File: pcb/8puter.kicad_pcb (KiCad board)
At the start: 2 copper layers, 180 x 120 mm, 80 parts, among them J1 PWR-DC, J2 DB9_Female, J3 USB_A, SW1 RESET_SW, U1 74AHC00, U10 74AC10, U11 74AC14, U12 W65C22NxPL, U13 MX25V8035F, U14 FT240XQ, U2 74AHC74, U3 DS1135Z, U4 74AHC32, U5 74AHC125, U6 MAX811MEUS-T, U7 STM8S003K3T, U8 74AHC00, U9 74AHC02

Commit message: Pivot to 6502
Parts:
- removed U1: 74AHC00, Package_SO:TSSOP-14_4.4x5mm_P0.65mm
- removed U10: 74AC10, Package_SO:TSSOP-14_4.4x5mm_P0.65mm
- removed U4: 74AHC32, Package_SO:TSSOP-14_4.4x5mm_P0.65mm
- removed U5: 74AHC125, Package_SO:TSSOP-14_4.4x5mm_P0.65mm
- removed U9: 74AHC02, Package_SO:TSSOP-14_4.4x5mm_P0.65mm
- added C24: 100nF, Capacitor_SMD:C_0603_1608Metric, F.Cu at (190.2, 91.3)
- added C25: 100nF, Capacitor_SMD:C_0603_1608Metric, F.Cu at (190.2, 89.5)
- added C26: 100nF, Capacitor_SMD:C_0603_1608Metric, F.Cu at (190.2, 87.7)
- added C27: 10nF, Capacitor_SMD:C_0603_1608Metric, F.Cu at (190.2, 85.9)
- added C28: 100nF, Capacitor_SMD:C_0603_1608Metric, F.Cu at (190.1, 84.2)
- added C29: 10nF, Capacitor_SMD:C_0603_1608Metric, F.Cu at (190.1, 82.4)
- added C30: 10nF, Capacitor_SMD:C_0603_1608Metric, F.Cu at (190.1, 80.7)
- added C31: 10nF, Capacitor_SMD:C_0603_1608Metric, F.Cu at (190.1, 78.8)
- added J4: FPGA_Prog, Connector_PinHeader_1.00mm:PinHeader_1x05_P1.00mm_Vertical, F.Cu at (181.8, 92.7)
- added PWREG1: LT1962-3.3, Package_SO:MSOP-8_3x3mm_P0.65mm, F.Cu at (108.8, 61.7)
- added R8: 4.7K, Resistor_SMD:R_0603_1608Metric, F.Cu at (184.0, 90.6)
- added R9: 1K, Resistor_SMD:R_0402_1005Metric, F.Cu at (182.4, 95.2)
- added U15: LCMXO2-256ZE-3SG32I, Package_DFN_QFN:QFN-32-1EP_5x5mm_P0.5mm_EP3.1x3.1mm, F.Cu at (176.5, 93.0)
- C1: value 1uF -> 10uF
- C19, C20: value 10nF -> 100nF; footprint Capacitor_SMD:C_0603_1608Metric -> Capacitor_THT:CP_Radial_D5.0mm_P2.00mm
- C21: value 10nF -> 100nF
- C5, C6: value 10nF -> 10uF; footprint Capacitor_SMD:C_0603_1608Metric -> Capacitor_THT:CP_Radial_D5.0mm_P2.00mm
- C7, C8: value 10nF -> 1uF; footprint Capacitor_SMD:C_0603_1608Metric -> Capacitor_THT:CP_Radial_D5.0mm_P2.00mm
- ROM1: value AT28HC256 -> AT28C256
- SRAM1: value KM62256CLP -> AS6C62256-55PCN
- U3: value DS1135Z -> DS1135Z-6+
- moved C8 109.7 mm to (88.2, 83.8), turned to -90 degrees
- moved C20 109.0 mm to (93.8, 60.7)
- moved C5 100.9 mm to (98.1, 83.5), turned to -90 degrees
- moved C19 100.7 mm to (103.3, 60.7)
- moved C7 94.2 mm to (115.8, 53.7), turned to -90 degrees
- moved C6 91.3 mm to (115.8, 61.2), turned to -90 degrees
- moved CRYSTAL0 79.9 mm to (192.1, 63.9), turned to 180 degrees
- moved C21 75.2 mm to (127.6, 65.3), turned to 0 degrees
- moved C11 74.3 mm to (130.8, 74.8)
- moved C18 71.3 mm to (132.0, 46.0)
- moved C2 68.4 mm to (132.1, 52.0), turned to 0 degrees
- moved C12 67.5 mm to (132.0, 57.2), turned to 0 degrees
- moved C14 66.0 mm to (113.0, 74.7)
- moved R4 60.0 mm to (142.0, 56.2), turned to 180 degrees
- moved R2 55.1 mm to (142.1, 53.3), turned to 180 degrees
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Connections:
- net Net-(D1-Pad1) renamed /Bus Control/RDY_R
- BDT1 pad 1: Net-(BDT1-Pad1) -> /Bus Control/CPU_W~{R}
- C17 pad 1: +5V -> Net-(C17-Pad1)
- C19 pad 1: +5V -> Net-(C19-Pad1)
- C20 pad 1: +5V -> Net-(C17-Pad1)
- C5 pad 1: +5V -> /Power/PWR
- C6 pad 1: +5V -> Net-(C19-Pad1)
- C7 pad 1: +5V -> Net-(C19-Pad1)
- C8 pad 1: +5V -> Net-(C17-Pad1)
- PWREG2 pad 1: +5V -> Net-(C17-Pad1)
- RP2 pad 2: ADDR11 -> ADDR8
- RP2 pad 3: ADDR10 -> ADDR9
- RP2 pad 4: ADDR9 -> ADDR11
- RP2 pad 5: ADDR8 -> ADDR10
- U12 pad 27: CLOCK -> /Peripheral Handler/CLK
- U2 pad 14: +5V -> (no net)
- U2 pad 7: GND -> (no net)
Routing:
- net ADDR19: track 136.2 -> 15.0 mm
- net ADDR18: track 131.1 -> 16.4 mm
- net CLOCK: track 127.1 -> 17.4 mm, vias 4 -> 0
- net ADDR17: track 125.7 -> 17.6 mm
- net ADDR16: track 120.9 -> 18.9 mm
- net /Bus Control/CLK=: track 107.0 -> 12.8 mm, vias 3 -> 0
- net ADDR15: track 104.0 -> 13.6 mm, vias 3 -> 0
- net +5V: track 77.5 -> 4.05 mm, vias 6 -> 0
- net BE: track 70.6 -> 7.28 mm, vias 2 -> 0
- net ADDR23: track 53.6 -> 10.2 mm, vias 2 -> 0
- net RDY: track 43.0 -> 0.00 mm, vias 2 -> 0
- net /Memory Unit/~{ERAM_CS0}: track 42.3 -> 0.00 mm
- net /Bus Control/CLK+: track 55.7 -> 14.6 mm, vias 2 -> 0
- net DATA0: track 85.6 -> 126.7 mm, vias 1 -> 4
- net ADDR22: track 50.4 -> 11.3 mm, vias 2 -> 0
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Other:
- outline, holes or cut-outs redrawn

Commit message: Serial interface
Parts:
- removed AD_DEC1: 74HCT154, Package_SO:SO-24_5.3x15mm_P1.27mm
- removed BDT1: 74AC245, Package_SO:TSSOP-20_4.4x6.5mm_P0.65mm
- removed C13, C14: 1uF, Capacitor_THT:CP_Radial_D8.0mm_P3.80mm
- removed C18: 100nF, Capacitor_SMD:C_1206_3216Metric_Pad1.33x1.80mm_HandSolder
- removed C21, C24, C25, C26, C28: 100nF, Capacitor_SMD:C_0603_1608Metric
- removed C22, C27, C29, C30, C31: 10nF, Capacitor_SMD:C_0603_1608Metric
- removed the C3 at (77.1, 74.2)
- removed the C3 at (87.1, 74.2)
- removed D1: 1N5817, Diode_THT:D_A-405_P7.62mm_Horizontal
- removed ERAM0, ERAM1, ERAM2, ERAM3: IS62WV10248, Package_SO:TSOP-II-44_10.16x18.41mm_P0.8mm
- removed J4: FPGA_Prog, Connector_PinHeader_1.00mm:PinHeader_1x05_P1.00mm_Vertical
- removed LATCH1: 74AC573, Package_SO:TSSOP-20_4.4x6.5mm_P0.65mm
- removed R12, R13, R14, R15, R16, R17, R18, R19, R20, R21, R22, R23, R32, R33, R34, R35, R6, R7: 1K, Resistor_SMD:R_0603_1608Metric
- removed R4, R5: 10K, Resistor_SMD:R_1206_3216Metric_Pad1.30x1.75mm_HandSolder
- removed R8: 4.7K, Resistor_SMD:R_0603_1608Metric
- removed R9: 1K, Resistor_SMD:R_0402_1005Metric
- removed RP1, RP2: 1K, Resistor_THT:R_Array_SIP9
- removed SRAM1: AS6C62256-55PCN, Package_DIP:DIP-28_W15.24mm
- removed SW1: RESET_SW, Button_Switch_THT:SW_PUSH_6mm_H13mm
- removed U11: 74AC14, Package_SO:TSSOP-14_4.4x5mm_P0.65mm
- removed U12: W65C22NxPL, Package_QFP:PQFP-44_10x10mm_P0.8mm
- removed U13: MX25V8035F, Package_SO:SOP-8_3.9x4.9mm_P1.27mm
- removed U14: FT240XQ, Package_DFN_QFN:QFN-24-1EP_4x4mm_P0.5mm_EP2.6x2.6mm
- removed U15: LCMXO2-256ZE-3SG32I, Package_DFN_QFN:QFN-32-1EP_5x5mm_P0.5mm_EP3.1x3.1mm
- removed U3: DS1135Z-6+, Package_SO:SO-8_5.3x6.2mm_P1.27mm
- removed U7: STM8S003K3T, Package_QFP:LQFP-32_7x7mm_P0.8mm
- removed U8: 74AHC00, Package_SO:TSSOP-14_4.4x5mm_P0.65mm
- added C3: 10uF 16V, Capacitor_THT:CP_Radial_D8.0mm_P5.00mm, F.Cu at (112.7, 47.8)
- added GLUE_FPGA1: LCMXO2-256-QFN32, Package_DFN_QFN:QFN-32-1EP_5x5mm_P0.5mm_EP3.1x3.1mm, F.Cu at (178.1, 114.8)
- added JTAG1: PIN_HDR, Connector_PinHeader_1.00mm:PinHeader_1x05_P1.00mm_Vertical, F.Cu at (183.8, 114.5)
- added PRP1: W65C22SxQ, Package_QFP:PQFP-44_10x10mm_P0.8mm, F.Cu at (184.6, 78.0)
- added RAM1: AS6C62256-55PCN, Package_DIP:DIP-28_W15.24mm_LongPads, F.Cu at (111.6, 121.1)
- added RESET_SW1: PUSHBTN, Button_Switch_THT:SW_PUSH_6mm_H13mm, F.Cu at (148.6, 58.8)
- added SERC1: W65C51NxQ, Package_QFP:LQFP-32_7x7mm_P0.8mm, F.Cu at (114.4, 68.9)
- added SERIAL1: Conn_2Rows-11Pins, Connector_PinHeader_1.00mm:PinHeader_2x06_P1.00mm_Vertical, F.Cu at (95.7, 64.0)
- added USB1: FT240XQ, Package_DFN_QFN:QFN-24-1EP_4x4mm_P0.5mm_EP2.6x2.6mm, F.Cu at (191.6, 55.9)
- added VIDEO1: STM32F301C6Tx, Package_QFP:LQFP-48_7x7mm_P0.5mm, F.Cu at (164.4, 54.0)
- C10, C11, C15, C16, C4, C9: footprint Capacitor_SMD:C_1206_3216Metric_Pad1.33x1.80mm_HandSolder -> Capacitor_SMD:C_0805_2012Metric
- C12: value 1uF -> 100nF; footprint Capacitor_SMD:C_1210_3225Metric_Pad1.33x2.70mm_HandSolder -> Capacitor_SMD:C_0805_2012Metric
- C17, C19, C20, C6, C7, C8: footprint Capacitor_THT:CP_Radial_D5.0mm_P2.00mm -> Capacitor_SMD:C_0805_2012Metric
- C2: footprint Capacitor_SMD:C_1210_3225Metric_Pad1.33x2.70mm_HandSolder -> Capacitor_SMD:C_0805_2012Metric
- C23: footprint Capacitor_SMD:C_1206_3216Metric -> Capacitor_SMD:C_0805_2012Metric
- CPU1: value W65C816SxP -> W65C02SxP
- J2: value DB9_Female -> DB15_Female; footprint Connector_Dsub:DSUB-9_Female_Horizontal_P2.77x2.84mm_EdgePinOffset9.90mm_Housed_MountingHolesOffset11.32mm -> Connector_Dsub:DSUB-15-HD_Female_Horizontal_P2.29x1.98mm_EdgePinOffset3.03mm_Housed_MountingHolesOffset4.94mm
- R1: footprint Resistor_SMD:R_0603_1608Metric -> Resistor_SMD:R_0805_2012Metric
- R2: footprint Resistor_SMD:R_1206_3216Metric_Pad1.30x1.75mm_HandSolder -> Resistor_SMD:R_0805_2012Metric
- R3: value 10K -> 4.7K; footprint Resistor_SMD:R_1206_3216Metric_Pad1.30x1.75mm_HandSolder -> Resistor_SMD:R_0805_2012Metric
- ROM1: footprint Package_DIP:DIP-28_W15.24mm_LongPads -> Package_DIP:DIP-28_W15.24mm_Socket_LongPads
- moved C5 100.2 mm to (190.2, 123.0)
- moved C19 99.2 mm to (191.2, 106.6), turned to 0 degrees
- moved PWREG1 98.1 mm to (189.3, 117.7), turned to -90 degrees
- moved C7 93.9 mm to (191.2, 109.6), turned to 0 degrees
- moved C6 91.3 mm to (191.2, 112.6), turned to 0 degrees
- moved C10 77.6 mm to (107.3, 67.7), turned to -90 degrees
- moved R2 77.2 mm to (119.4, 127.1), turned to 0 degrees
- moved C9 76.8 mm to (141.0, 51.7), turned to 0 degrees
- moved CRYSTAL0 74.7 mm to (121.4, 39.8), turned to -90 degrees
- moved R3 67.7 mm to (186.1, 112.3), turned to 90 degrees
- moved C23 63.0 mm to (196.2, 55.6), turned to -90 degrees
- moved R1 55.9 mm to (182.3, 118.9)
- moved U2 53.5 mm to (137.2, 55.7), turned to 0 degrees
- moved J2 46.0 mm to (158.4, 43.2)
- moved C2 39.9 mm to (143.2, 90.3), turned to 90 degrees
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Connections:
- net RESET renamed ~{RESET}
- C10 pad 1: +5V -> GND
- C10 pad 2: GND -> +5V
- C12 pad 1: +5V -> GND
- C12 pad 2: GND -> +5V
- C19 pad 1: Net-(C19-Pad1) -> +3V3
- C5 pad 1: /Power/PWR -> +5V
- C6 pad 1: Net-(C19-Pad1) -> +3V3
- C7 pad 1: Net-(C19-Pad1) -> +3V3
- CPU1 pad 26: /DBA7 -> DATA7
- CPU1 pad 27: /DBA6 -> DATA6
- CPU1 pad 28: /DBA5 -> DATA5
- CPU1 pad 29: /DBA4 -> DATA4
- CPU1 pad 3: Net-(CPU1-Pad3) -> unconnected-(CPU1-Pad3)
- CPU1 pad 30: /DBA3 -> DATA3
- CPU1 pad 31: /DBA2 -> DATA2
- CPU1 pad 32: /DBA1 -> DATA1
- CPU1 pad 33: /DBA0 -> DATA0
- CPU1 pad 35: EMU -> unconnected-(CPU1-Pad35)
- CPU1 pad 38: unconnected-(CPU1-Pad38) -> +5V
- CPU1 pad 39: VDA -> unconnected-(CPU1-Pad39)
- CPU1 pad 7: VPA -> unconnected-(CPU1-Pad7)
- J3 pad 2: unconnected-(J3-Pad2) -> Net-(J3-Pad2)
- J3 pad 3: unconnected-(J3-Pad3) -> Net-(J3-Pad3)
- J3 pad 4: unconnected-(J3-Pad4) -> GND
- J3 pad 5: unconnected-(J3-Pad5) -> GND
- PWREG1 pad 1: Net-(C19-Pad1) -> +3V3
- PWREG1 pad 4: unconnected-(PWREG1-Pad4) -> GND
- PWREG1 pad 8: /Power/PWR -> +5V
- R1 pad 1: +5V -> Net-(R1-Pad1)
- R1 pad 2: RDY -> +3V3
- R3 pad 1: +5V -> /TCK
- R3 pad 2: Net-(R3-Pad2) -> GND
- ROM1 pad 20: /Memory Unit/~{ROM_CS} -> ~{RAM_CS}
- ROM1 pad 22: ~{READ} -> CPU_W~{R}
- U2 pad 11: /Clock/CRYSTAL -> GND
- U2 pad 12: ~{CLOCK} -> GND
- U2 pad 14: (no net) -> +5V
- U2 pad 2: Net-(R3-Pad2) -> ~{CLOCK}
- U2 pad 3: /Bus Control/CLK= -> /Clock/CRYSTAL
- U2 pad 5: /Bus Control/RDY_R -> CLOCK
- U2 pad 6: /Bus Control/~{RDY_R} -> ~{CLOCK}
- U2 pad 7: (no net) -> GND
- U2 pad 8: ~{CLOCK} -> unconnected-(U2-Pad8)
- U2 pad 9: CLOCK -> unconnected-(U2-Pad9)
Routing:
- net CPU_R~{W}: track 6.61 -> 185.1 mm, vias 0 -> 2
- net ADDR1: track 0.00 -> 176.1 mm, vias 0 -> 3
- net ADDR0: track 0.00 -> 173.2 mm, vias 0 -> 3
- net ~{SERIAL_CS}: track 0.00 -> 166.8 mm, vias 0 -> 4
- net CPU_W~{R}: track 0.00 -> 147.3 mm, vias 0 -> 3
- net ~{ROM_CS}: track 0.00 -> 143.5 mm, vias 0 -> 2
- net ADDR10: track 0.00 -> 139.0 mm, vias 0 -> 4
- net ADDR11: track 0.00 -> 130.4 mm, vias 0 -> 4
- net ADDR9: track 0.00 -> 125.3 mm, vias 0 -> 4
- net ~{RAM_CS}: track 0.00 -> 121.9 mm, vias 0 -> 2
- net ADDR15: track 13.6 -> 130.2 mm, vias 0 -> 3
- net ADDR13: track 7.78 -> 120.5 mm, vias 0 -> 3
- net ADDR8: track 0.00 -> 112.2 mm, vias 0 -> 4
- net ADDR2: track 0.00 -> 100.3 mm, vias 0 -> 1
- net ADDR3: track 0.00 -> 94.9 mm, vias 0 -> 1
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- added copper zone on B.Cu, net +5V
- added copper zone on F.Cu, net GND
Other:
- board size 180 x 120 mm -> 120 x 100 mm

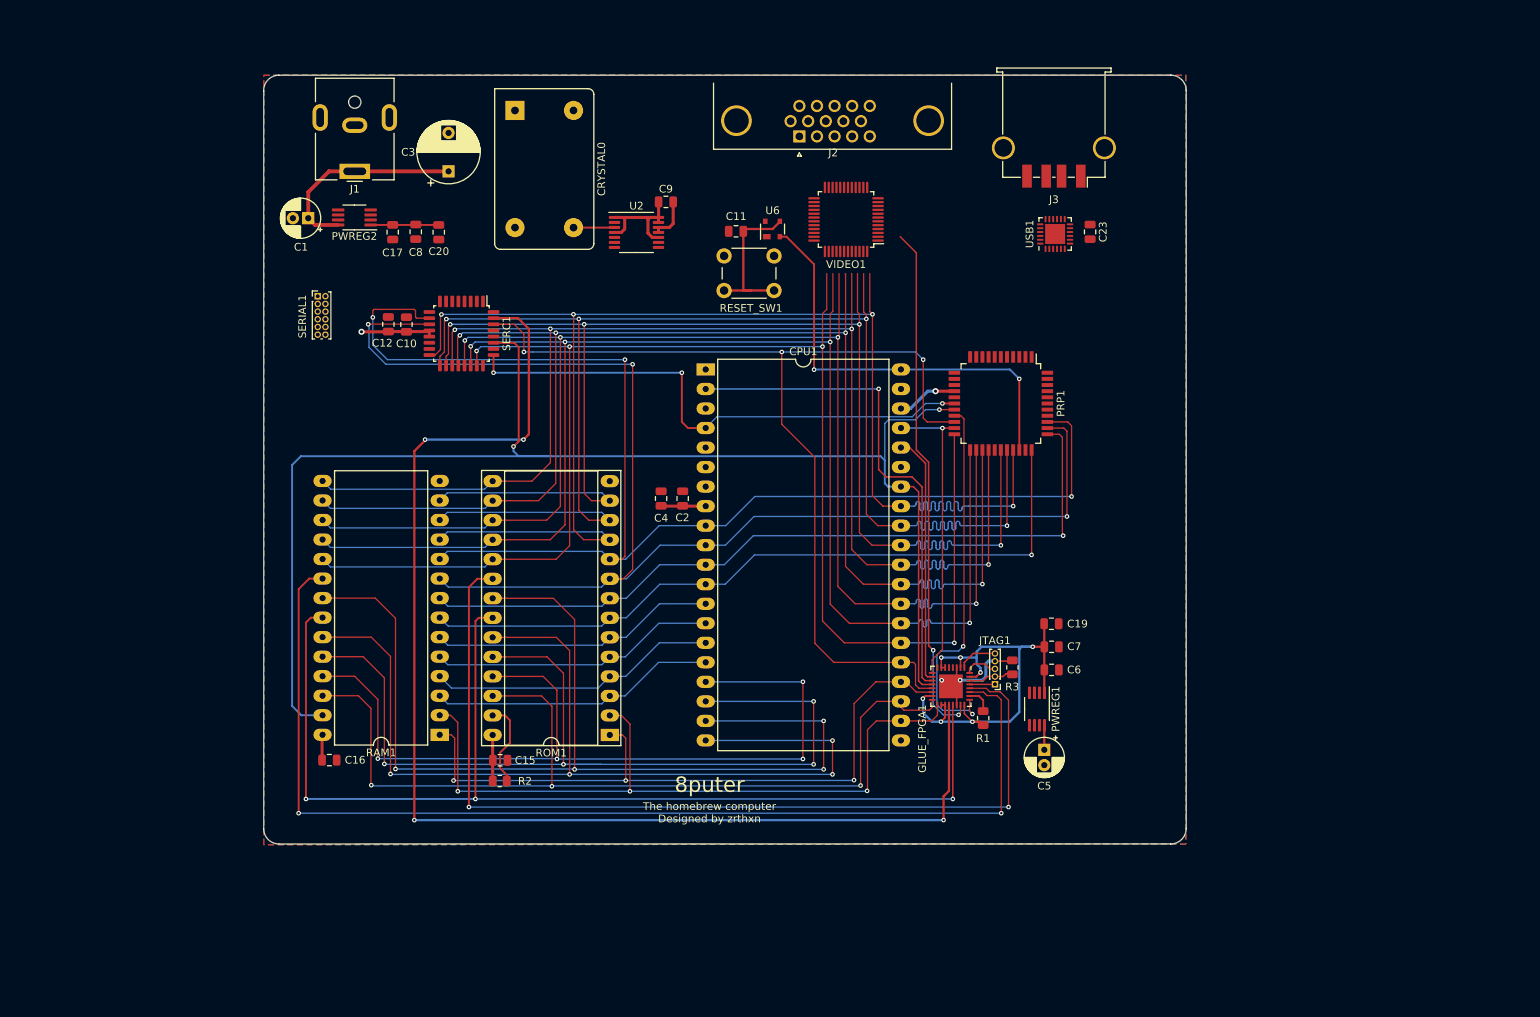
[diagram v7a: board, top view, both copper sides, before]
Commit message: Serial, debug and prph headers
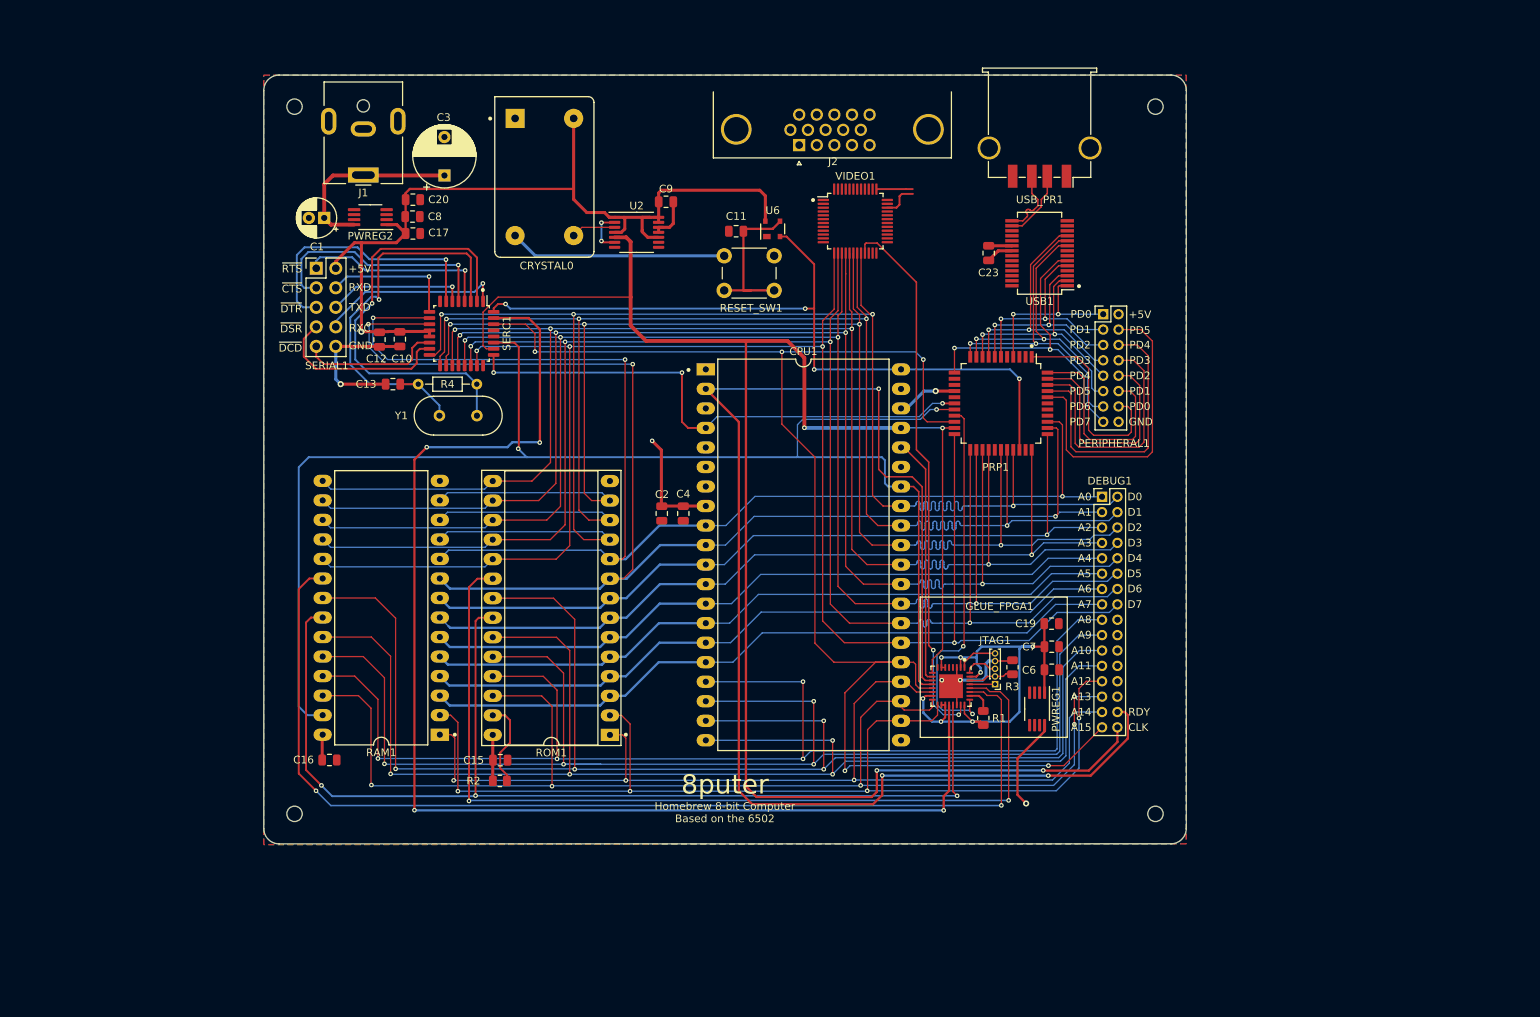
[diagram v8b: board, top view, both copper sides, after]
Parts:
- removed C5: 10uF, Capacitor_THT:CP_Radial_D5.0mm_P2.00mm
- removed J3: USB_A, Connector_USB:USB_A_TE_292303-7_Horizontal
- added C13: 30pF, Capacitor_SMD:C_0805_2012Metric, F.Cu at (105.5, 75.4)
- added DEBUG1: Conn_02x16_Odd_Even, Connector_PinHeader_2.00mm:PinHeader_2x16_P2.00mm_Vertical, F.Cu at (197.7, 90.1)
- added PERIPHERAL1: Conn_02x08_Odd_Even, Connector_PinHeader_2.00mm:PinHeader_2x08_P2.00mm_Vertical, F.Cu at (197.9, 66.3)
- added R4: 1M, Resistor_THT:R_Axial_DIN0204_L3.6mm_D1.6mm_P7.62mm_Horizontal, F.Cu at (116.4, 75.4)
- added USB_PR1: USB_A, Connector_USB:USB_A_TE_292303-7_Horizontal, F.Cu at (189.6, 42.0)
- added Y1: 1.8432MHz, Crystal:Crystal_HC49-4H_Vertical, F.Cu at (111.5, 79.5)
- SERIAL1: value Conn_2Rows-11Pins -> Conn_02x05_Odd_Even; footprint Connector_PinHeader_1.00mm:PinHeader_2x06_P1.00mm_Vertical -> Connector_PinHeader_2.54mm:PinHeader_2x05_P2.54mm_Vertical
- USB1: value FT240XQ -> FT245RL; footprint Package_DFN_QFN:QFN-24-1EP_4x4mm_P0.5mm_EP2.6x2.6mm -> Package_SO:SSOP-28_5.3x10.2mm_P0.65mm
- moved C23 13.5 mm to (183.0, 58.4)
- moved C20 5.41 mm to (108.1, 51.4), turned to 0 degrees
- moved SERIAL1 3.64 mm to (95.5, 60.4)
- moved C4 3.48 mm to (143.3, 92.3), turned to -90 degrees
- moved C2 3.34 mm to (140.5, 92.3), turned to -90 degrees
- moved USB1 3.22 mm to (189.6, 58.4), turned to 180 degrees
- moved C17 2.64 mm to (108.1, 55.8), turned to 0 degrees
- moved C12 2.30 mm to (103.7, 69.6), turned to 90 degrees
- moved C10 2.09 mm to (106.4, 69.6), turned to 90 degrees
- moved C1 2.08 mm to (96.6, 53.8)
- moved PWREG2 2.08 mm to (102.6, 53.7)
- moved C8 2.02 mm to (108.0, 53.6), turned to 0 degrees
- moved VIDEO1 1.22 mm to (165.6, 54.2), turned to 0 degrees
- moved J1 1.22 mm to (101.6, 48.2)
- moved J2 1.13 mm to (158.3, 44.3)
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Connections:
- C17 pad 1: Net-(C17-Pad1) -> +5V
- C20 pad 1: Net-(C17-Pad1) -> +5V
- C8 pad 1: Net-(C17-Pad1) -> +5V
- PRP1 pad 1: unconnected-(PRP1-Pad1) -> /Peripheral Handler/PC5
- PRP1 pad 2: unconnected-(PRP1-Pad2) -> Net-(PRP1-Pad2)
- PRP1 pad 3: unconnected-(PRP1-Pad3) -> Net-(PRP1-Pad3)
- PRP1 pad 40: unconnected-(PRP1-Pad40) -> /Peripheral Handler/PC0
- PRP1 pad 41: unconnected-(PRP1-Pad41) -> /Peripheral Handler/PC1
- PRP1 pad 42: unconnected-(PRP1-Pad42) -> /Peripheral Handler/PC2
- PRP1 pad 43: unconnected-(PRP1-Pad43) -> /Peripheral Handler/PC3
- PRP1 pad 44: unconnected-(PRP1-Pad44) -> /Peripheral Handler/PC4
- PWREG2 pad 1: Net-(C17-Pad1) -> +5V
- SERC1 pad 1: unconnected-(SERC1-Pad1) -> Net-(SERC1-Pad1)
- SERC1 pad 14: unconnected-(SERC1-Pad14) -> Net-(SERC1-Pad14)
- SERC1 pad 15: unconnected-(SERC1-Pad15) -> Net-(SERC1-Pad15)
- SERC1 pad 2: unconnected-(SERC1-Pad2) -> Net-(R4-Pad1)
- SERC1 pad 3: unconnected-(SERC1-Pad3) -> Net-(C13-Pad1)
- SERC1 pad 4: unconnected-(SERC1-Pad4) -> Net-(SERC1-Pad4)
- SERC1 pad 5: unconnected-(SERC1-Pad5) -> Net-(SERC1-Pad5)
- SERC1 pad 6: unconnected-(SERC1-Pad6) -> Net-(SERC1-Pad6)
- SERC1 pad 7: unconnected-(SERC1-Pad7) -> Net-(SERC1-Pad7)
- SERC1 pad 9: unconnected-(SERC1-Pad9) -> Net-(SERC1-Pad9)
- SERIAL1 pad 1: unconnected-(SERIAL1-Pad1) -> Net-(SERC1-Pad4)
- SERIAL1 pad 10: unconnected-(SERIAL1-Pad10) -> GND
- SERIAL1 pad 2: unconnected-(SERIAL1-Pad2) -> +5V
- SERIAL1 pad 3: unconnected-(SERIAL1-Pad3) -> Net-(SERC1-Pad5)
- SERIAL1 pad 4: unconnected-(SERIAL1-Pad4) -> Net-(SERC1-Pad9)
- SERIAL1 pad 5: unconnected-(SERIAL1-Pad5) -> Net-(SERC1-Pad7)
- SERIAL1 pad 6: unconnected-(SERIAL1-Pad6) -> Net-(SERC1-Pad6)
- SERIAL1 pad 7: unconnected-(SERIAL1-Pad7) -> Net-(SERC1-Pad15)
- SERIAL1 pad 8: unconnected-(SERIAL1-Pad8) -> Net-(SERC1-Pad1)
- SERIAL1 pad 9: unconnected-(SERIAL1-Pad9) -> Net-(SERC1-Pad14)
- USB1 pad 1: /Peripheral Handler/PD1 -> /Peripheral Handler/PD0
- USB1 pad 10: Net-(J3-Pad3) -> /Peripheral Handler/PD6
- USB1 pad 11: Net-(J3-Pad2) -> /Peripheral Handler/PD3
- USB1 pad 12: Net-(USB1-Pad12) -> unconnected-(USB1-Pad12)
- USB1 pad 13: ~{RESET} -> unconnected-(USB1-Pad13)
- USB1 pad 15: +5V -> /Peripheral Handler/SUSB+
- USB1 pad 16: GND -> /Peripheral Handler/SUSB-
- USB1 pad 18: unconnected-(USB1-Pad18) -> GND
- USB1 pad 2: /Peripheral Handler/PD7 -> /Peripheral Handler/PD4
- USB1 pad 20: unconnected-(USB1-Pad20) -> +5V
- USB1 pad 21: /Peripheral Handler/PD0 -> GND
- USB1 pad 22: /Peripheral Handler/PD4 -> unconnected-(USB1-Pad22)
- USB1 pad 23: /Peripheral Handler/PD2 -> unconnected-(USB1-Pad23)
- USB1 pad 24: Net-(USB1-Pad12) -> unconnected-(USB1-Pad24)
- USB1 pad 25: GND -> unconnected-(USB1-Pad25)
- USB1 pad 3: GND -> /Peripheral Handler/PD2
- USB1 pad 4: /Peripheral Handler/PD5 -> unconnected-(USB1-Pad4)
- USB1 pad 5: /Peripheral Handler/PD6 -> /Peripheral Handler/PD1
- USB1 pad 6: /Peripheral Handler/PD3 -> /Peripheral Handler/PD7
- USB1 pad 7: unconnected-(USB1-Pad7) -> GND
- USB1 pad 9: unconnected-(USB1-Pad9) -> /Peripheral Handler/PD5
- VIDEO1 pad 13: unconnected-(VIDEO1-Pad13) -> DATA7
- VIDEO1 pad 14: unconnected-(VIDEO1-Pad14) -> DATA6
- VIDEO1 pad 15: unconnected-(VIDEO1-Pad15) -> DATA5
- VIDEO1 pad 16: unconnected-(VIDEO1-Pad16) -> DATA4
- VIDEO1 pad 17: unconnected-(VIDEO1-Pad17) -> DATA3
- VIDEO1 pad 18: DATA0 -> DATA2
- VIDEO1 pad 2: ~{VID_CS} -> unconnected-(VIDEO1-Pad2)
- VIDEO1 pad 20: DATA2 -> DATA0
- VIDEO1 pad 21: unconnected-(VIDEO1-Pad21) -> ~{VID_CS}
- VIDEO1 pad 39: DATA3 -> unconnected-(VIDEO1-Pad39)
- VIDEO1 pad 40: DATA4 -> unconnected-(VIDEO1-Pad40)
- VIDEO1 pad 41: DATA5 -> unconnected-(VIDEO1-Pad41)
- VIDEO1 pad 42: DATA6 -> unconnected-(VIDEO1-Pad42)
- VIDEO1 pad 43: DATA7 -> unconnected-(VIDEO1-Pad43)
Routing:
- net CLOCK: track 39.4 -> 237.9 mm, vias 1 -> 4
- net RDY: track 65.9 -> 180.9 mm, vias 1 -> 3
- net +5V: track 51.1 -> 162.8 mm, vias 2 -> 4
- net Net-(R4-Pad1): track 0.00 -> 55.7 mm, vias 0 -> 1
- net ADDR15: track 130.2 -> 185.0 mm, vias 3 -> 5
- net ADDR7: track 37.3 -> 92.1 mm
- net ADDR8: track 112.2 -> 166.9 mm
- net ADDR5: track 37.3 -> 91.5 mm
- net ADDR4: track 37.3 -> 91.5 mm
- net ADDR6: track 37.7 -> 91.9 mm
- net Net-(C13-Pad1): track 0.00 -> 52.2 mm, vias 0 -> 1
- net ADDR9: track 125.3 -> 177.1 mm
- net GND: track 20.2 -> 71.4 mm, vias 2 -> 3
- net ADDR10: track 139.0 -> 188.2 mm
- net ADDR11: track 130.4 -> 177.2 mm
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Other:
- outline, holes or cut-outs redrawn
- board text added: "+5V"
- board text added: "8puter Homebrew Computer"
- board text added: "A0"
- board text added: "A1"
- board text added: "A10"
- board text added: "A11"
- board text added: "A12"
- board text added: "A13"
- board text added: "A14"
- board text added: "A15"
- board text added: "A2"
- board text added: "A3"
- board text added: "A4"
- board text added: "A5"
- board text added: "A6"
- board text added: "A7"
- board text added: "A8"
- board text added: "A9"
- board text added: "ADDR BUS"
- board text added: "CLK"
- board text added: "D0"
- board text added: "D1"
- board text added: "D2"
- board text added: "D3"
- board text added: "D4"
- board text added: "D5"
- board text added: "D6"
- board text added: "D7"
- board text added: "DATA BUS"
- board text added: "GND"
- board text added: "Homebrew 8-bit Computer Based on the 6502"
- board text added: "PD0"
- board text added: "PD1"
- board text added: "PD2"
- board text added: "PD3"
- board text added: "PD4"
- board text added: "PD5"
- board text added: "PD6"
- board text added: "PD7"
- board text added: "RDY"
- board text added: "RXC"
- board text added: "RXD"
- board text added: "Revision 1 | Apr 2022 Design by zrthxn"
- board text added: "TXD"
- board text added: "~{CTS}"
- board text added: "~{DCD}"
- board text added: "~{DSR}"
- board text added: "~{DTR}"
- board text added: "~{RTS}"
- board text removed: "The homebrew computer Designed by zrthxn"
